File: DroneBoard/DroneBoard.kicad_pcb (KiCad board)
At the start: 2 copper layers, 57 x 42 mm, 51 parts, among them J1 USB4105-GF-A, J2 Conn_01x02, SW1 1825910-6, SW2 1825910-6, U1 ICM-20608-G, U2 ESP32-S3-WROOM-1-N16, U3 TPS63051RMWR

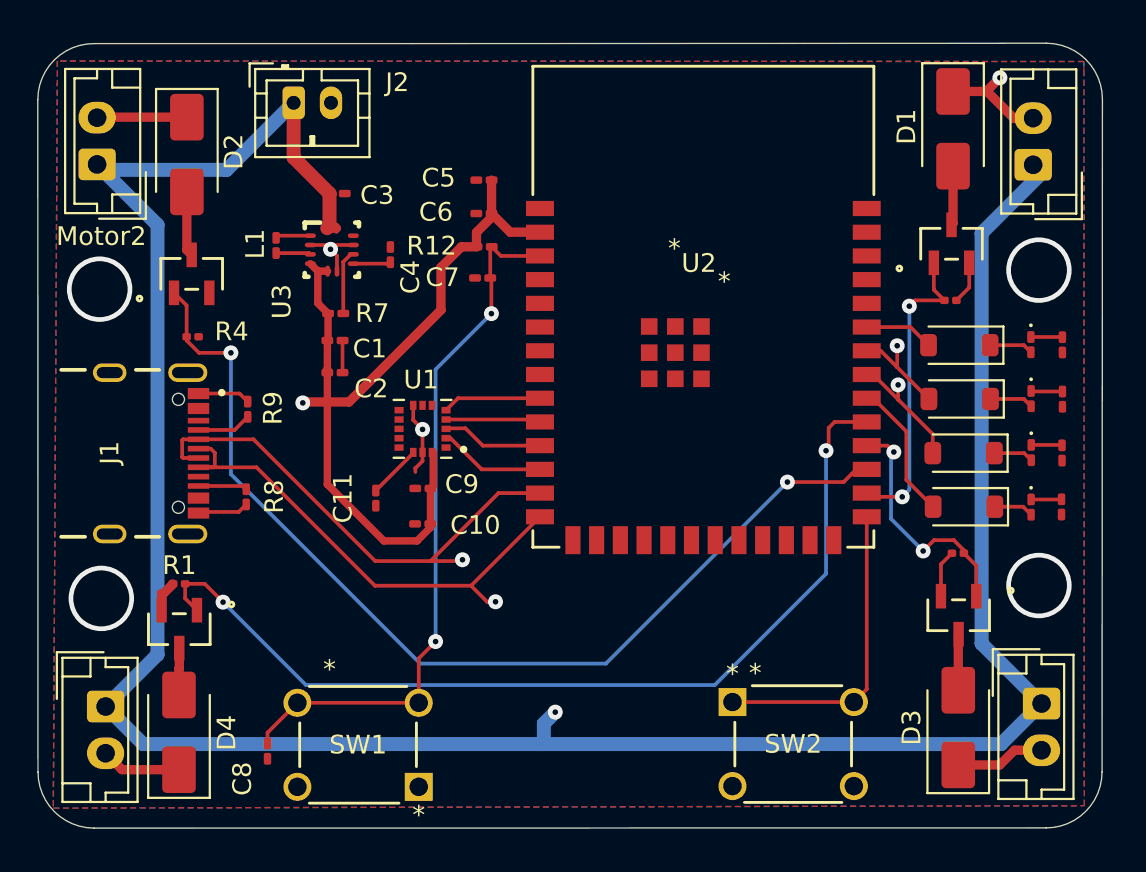
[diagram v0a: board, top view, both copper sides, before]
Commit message: Fixed Schematics
Fixed the flyback diodes
Fixed the LED resistors and extra diodes
Fixed the 0603 sizings
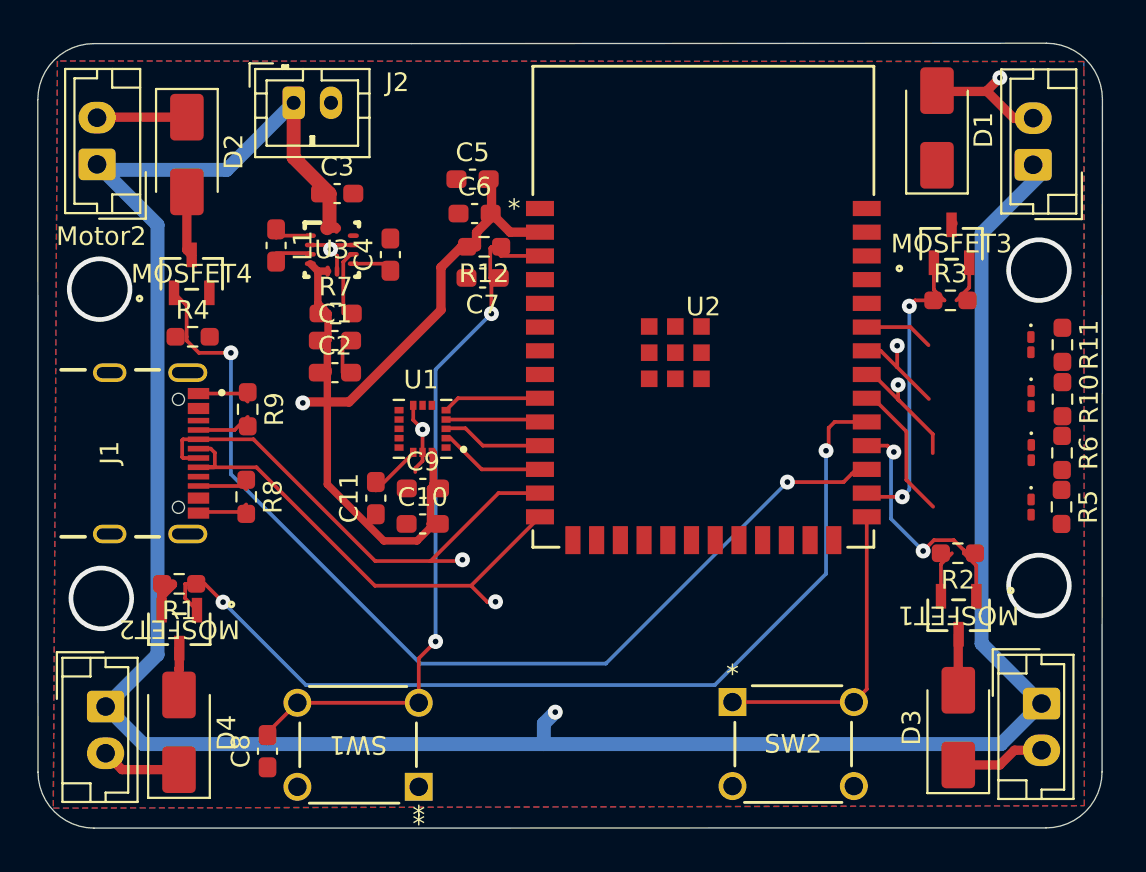
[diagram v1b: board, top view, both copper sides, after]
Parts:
- removed D10, D5, D6, D9: 1N4148W, Diode_SMD:D_SOD-123
- C1, C10, C11, C2, C3, C4, C5, C6, C7, C8, C9, L1: footprint Capacitor_SMD:C_0201_0603Metric_Pad0.64x0.40mm_HandSolder -> Capacitor_SMD:C_0603_1608Metric_Pad1.08x0.95mm_HandSolder
- R1, R2, R3, R4: footprint Resistor_SMD:R_0201_0603Metric -> Resistor_SMD:R_0603_1608Metric_Pad0.98x0.95mm_HandSolder
- R10, R11, R5, R6: value 10k -> 430; footprint Resistor_SMD:R_0201_0603Metric_Pad0.64x0.40mm_HandSolder -> Resistor_SMD:R_0603_1608Metric_Pad0.98x0.95mm_HandSolder
- R12, R7, R8: footprint Resistor_SMD:R_0201_0603Metric_Pad0.64x0.40mm_HandSolder -> Resistor_SMD:R_0603_1608Metric_Pad0.98x0.95mm_HandSolder
- R9: value 5.1 -> 5.1k; footprint Resistor_SMD:R_0201_0603Metric_Pad0.64x0.40mm_HandSolder -> Resistor_SMD:R_0603_1608Metric_Pad0.98x0.95mm_HandSolder
- moved D1 0.86 mm to (137.2, 73.5), turned to 90 degrees
- moved C5 0.61 mm to (112.3, 76.3)
- moved C6 0.50 mm to (112.4, 78.1)
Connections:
- D1 pad 1: Net-(D1-K) -> VAA
- D2 pad 1: Net-(D2-K) -> VAA
- D3 pad 1: Net-(D3-K) -> VAA
- D4 pad 1: Net-(D4-K) -> VAA
- LED1 pad 2: Net-(D5-K) -> LED_1
- LED2 pad 2: Net-(D6-K) -> LED_2
- LED3 pad 2: Net-(D9-K) -> LED_3
- LED4 pad 2: Net-(D10-K) -> LED_4
- Motor1 pad 2: Net-(D1-K) -> Net-(D1-A)
- Motor2 pad 2: Net-(D2-K) -> Net-(D2-A)
- Motor3 pad 2: Net-(D3-K) -> Net-(D3-A)
- Motor4 pad 2: Net-(D4-K) -> Net-(D4-A)
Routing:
- net (no net): track 0.00 -> 13.9 mm
- net Net-(D1-K): track 5.90 -> 0.00 mm, vias 1 -> 0
- net Net-(D2-K): track 4.82 -> 0.00 mm
- net Net-(D3-K): track 4.79 -> 0.00 mm
- net Net-(D4-K): track 4.29 -> 0.00 mm
- net Net-(D1-A): track 3.17 -> 6.01 mm, vias 0 -> 1
- net Net-(D9-K): track 2.36 -> 0.00 mm
- net Net-(D10-K): track 2.35 -> 0.00 mm
- net Net-(D5-K): track 2.18 -> 0.00 mm
- net Net-(D6-K): track 2.17 -> 0.00 mm
- net Net-(LED4-K): track 1.69 -> 0.00 mm
- net Net-(LED2-K): track 1.66 -> 0.00 mm
- net Net-(LED3-K): track 1.69 -> 0.04 mm
- net Net-(LED1-K): track 1.63 -> 0.00 mm

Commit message: Routing and some small schematic updates
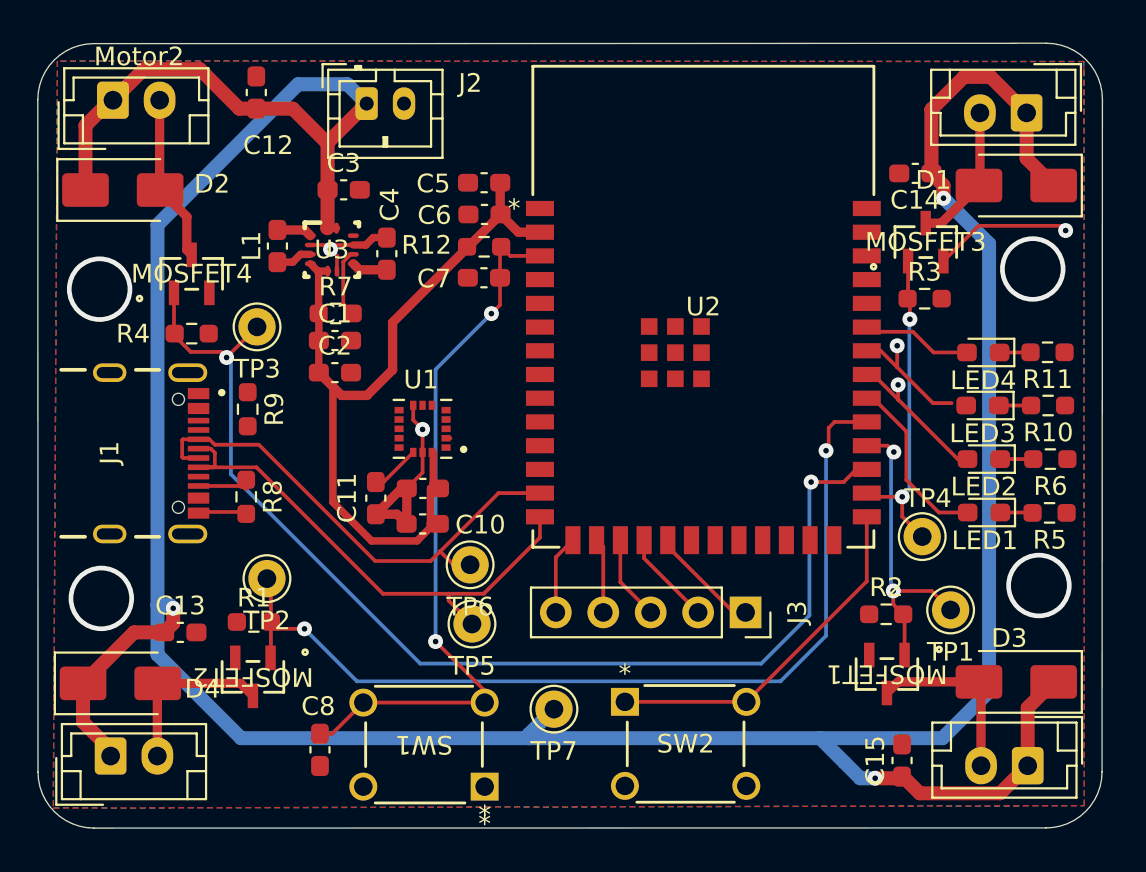
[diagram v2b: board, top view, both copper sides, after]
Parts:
- added C12: 47μF, Capacitor_SMD:C_0603_1608Metric_Pad1.08x0.95mm_HandSolder, F.Cu at (100.7, 71.6)
- added C13: 47μF, Capacitor_SMD:C_0603_1608Metric_Pad1.08x0.95mm_HandSolder, F.Cu at (96.6, 100.5)
- added C14: 47μF, Capacitor_SMD:C_0603_1608Metric_Pad1.08x0.95mm_HandSolder, F.Cu at (136.0, 76.0)
- added C15: 47μF, Capacitor_SMD:C_0603_1608Metric_Pad1.08x0.95mm_HandSolder, F.Cu at (135.3, 107.4)
- added J3: Conn_01x05, Connector_PinSocket_2.54mm:PinSocket_1x05_P2.54mm_Vertical, F.Cu at (126.9, 99.5)
- added TP1: TestPoint, Connector_Pin:Pin_D1.0mm_L10.0mm, F.Cu at (137.9, 99.3)
- added TP2: TestPoint, Connector_Pin:Pin_D1.0mm_L10.0mm, F.Cu at (101.3, 97.7)
- added TP3: TestPoint, Connector_Pin:Pin_D1.0mm_L10.0mm, F.Cu at (100.7, 84.2)
- added TP4: TestPoint, Connector_Pin:Pin_D1.0mm_L10.0mm, F.Cu at (136.4, 95.4)
- added TP5: TestPoint, Connector_Pin:Pin_D1.0mm_L10.0mm, F.Cu at (112.2, 100.1)
- added TP6: TestPoint, Connector_Pin:Pin_D1.0mm_L10.0mm, F.Cu at (112.2, 96.9)
- added TP7: TestPoint, Connector_Pin:Pin_D1.0mm_L10.0mm, F.Cu at (116.6, 104.7)
- LED1, LED2, LED3, LED4: footprint LED_SMD:LED_0201_0603Metric_Pad0.64x0.40mm_HandSolder -> LED_SMD:LED_0603_1608Metric_Pad1.05x0.95mm_HandSolder
- moved SW2 5.76 mm to (126.9, 108.8)
- moved D1 5.25 mm to (141.4, 76.6), turned to 180 degrees
- moved R2 5.04 mm to (134.4, 99.6)
- moved MOSFET1 4.97 mm to (134.5, 102.8)
- moved MOSFET2 4.70 mm to (100.5, 102.9)
- moved R1 4.49 mm to (100.6, 100.0)
- moved D4 4.09 mm to (93.4, 103.3), turned to 0 degrees
- moved D3 3.96 mm to (141.4, 103.2), turned to 180 degrees
- moved D2 3.92 mm to (93.6, 76.8), turned to 0 degrees
- moved J2 3.91 mm to (106.6, 72.2)
- moved Motor2 3.54 mm to (93.0, 72.0), turned to 0 degrees
- moved SW1 3.53 mm to (106.4, 104.3)
- moved Motor3 3.41 mm to (142.0, 107.7), turned to 180 degrees
- moved C8 2.81 mm to (104.1, 106.8)
- moved Motor1 2.80 mm to (141.9, 72.7), turned to 180 degrees
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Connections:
- U2 pad 15: unconnected-(U2-IO3-Pad15) -> Net-(J3-Pin_5)
- U2 pad 16: unconnected-(U2-IO46-Pad16) -> Net-(J3-Pin_4)
- U2 pad 17: unconnected-(U2-IO9-Pad17) -> Net-(J3-Pin_3)
- U2 pad 18: unconnected-(U2-IO10-Pad18) -> Net-(J3-Pin_2)
- U2 pad 19: unconnected-(U2-IO11-Pad19) -> Net-(J3-Pin_1)
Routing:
- net VAA: track 137.2 -> 189.8 mm, vias 1 -> 3
- net (no net): track 13.9 -> 0.00 mm
- net Net-(D4-A): track 2.51 -> 9.27 mm
- net Net-(D3-A): track 3.01 -> 9.71 mm
- net Motor_2_PWM: track 54.5 -> 60.9 mm
- net Net-(J3-Pin_1): track 0.00 -> 5.97 mm
- net IMU_SCLK: track 5.72 -> 0.24 mm
- net IMU_SDI: track 5.43 -> 0.04 mm
- net IMU_CS: track 5.29 -> 0.00 mm
- net Net-(D2-A): track 3.82 -> 8.99 mm
- net Net-(J3-Pin_2): track 0.00 -> 5.07 mm
- net IMU_SDO: track 5.08 -> 0.18 mm
- net GND: track 21.6 -> 26.4 mm, vias 2 -> 3
- net Net-(J3-Pin_3): track 0.00 -> 4.54 mm
- net Net-(J3-Pin_5): track 0.00 -> 4.25 mm
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
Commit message: Mostly Routing and Power over USBC
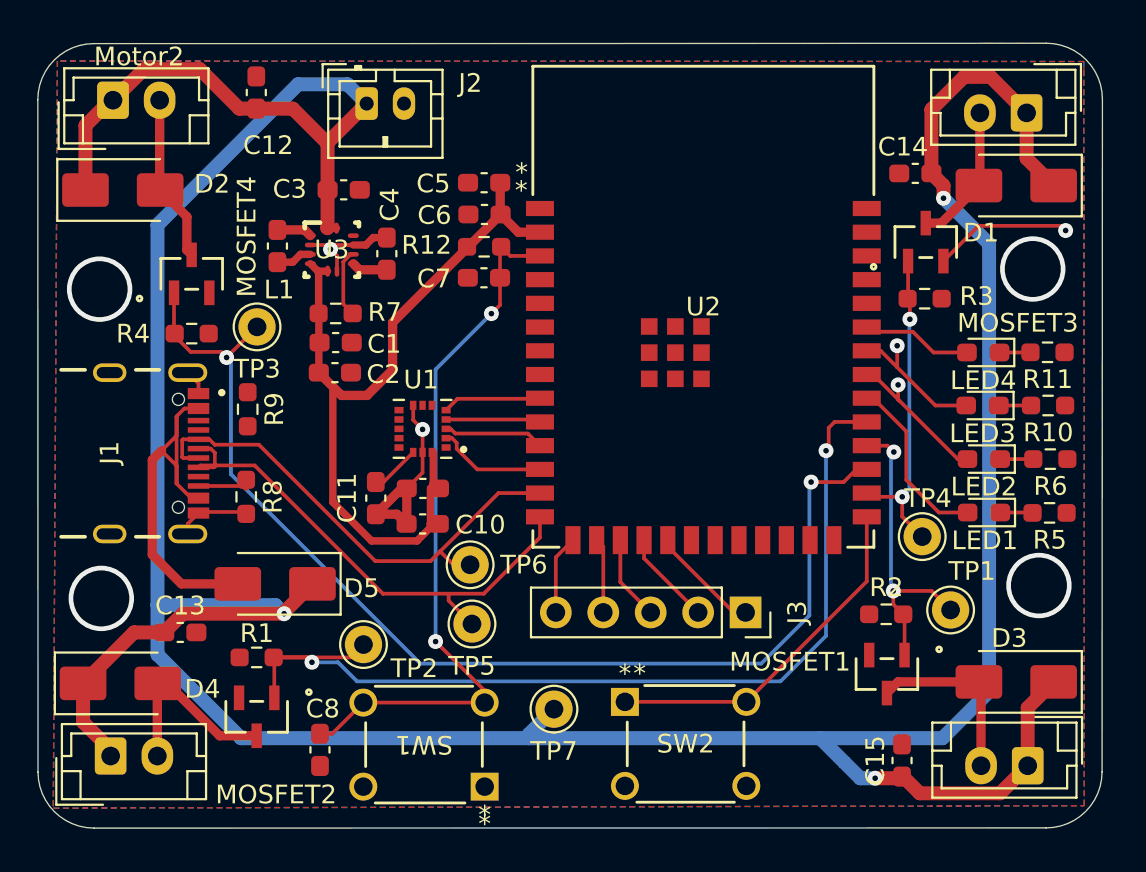
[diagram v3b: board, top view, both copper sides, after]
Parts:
- added D5: 1N4007, Diode_SMD:D_SMA, F.Cu at (101.7, 97.9)
- moved TP2 6.26 mm to (106.4, 101.2)
- moved MOSFET2 2.15 mm to (100.7, 105.1)
- moved R1 1.91 mm to (100.7, 101.9)
- moved C1 0.12 mm to (105.0, 85.0)
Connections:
- J1 pad A4_B9: unconnected-(J1-VBUS-PadA4_B9) -> Net-(D5-A)
- J1 pad B4_A9: unconnected-(J1-VBUS__1-PadB4_A9) -> Net-(D5-A)
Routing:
- net Net-(D5-A): track 0.00 -> 21.8 mm
- net VAA: track 189.8 -> 203.4 mm
- net IMU_SCLK: track 0.24 -> 5.91 mm
- net IMU_SDI: track 0.04 -> 5.44 mm
- net IMU_CS: track 0.00 -> 5.29 mm
- net IMU_SDO: track 0.18 -> 5.08 mm
- net GND: track 26.4 -> 29.1 mm
- net Motor_4_PWM: track 49.8 -> 52.0 mm
- net Net-(D4-A): track 9.27 -> 10.4 mm
- net LED_3: track 6.85 -> 7.68 mm
